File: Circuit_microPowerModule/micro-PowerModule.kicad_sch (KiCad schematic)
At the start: 9 parts, among them J101 Screw_Terminal_01x02, J102 Jack-DC

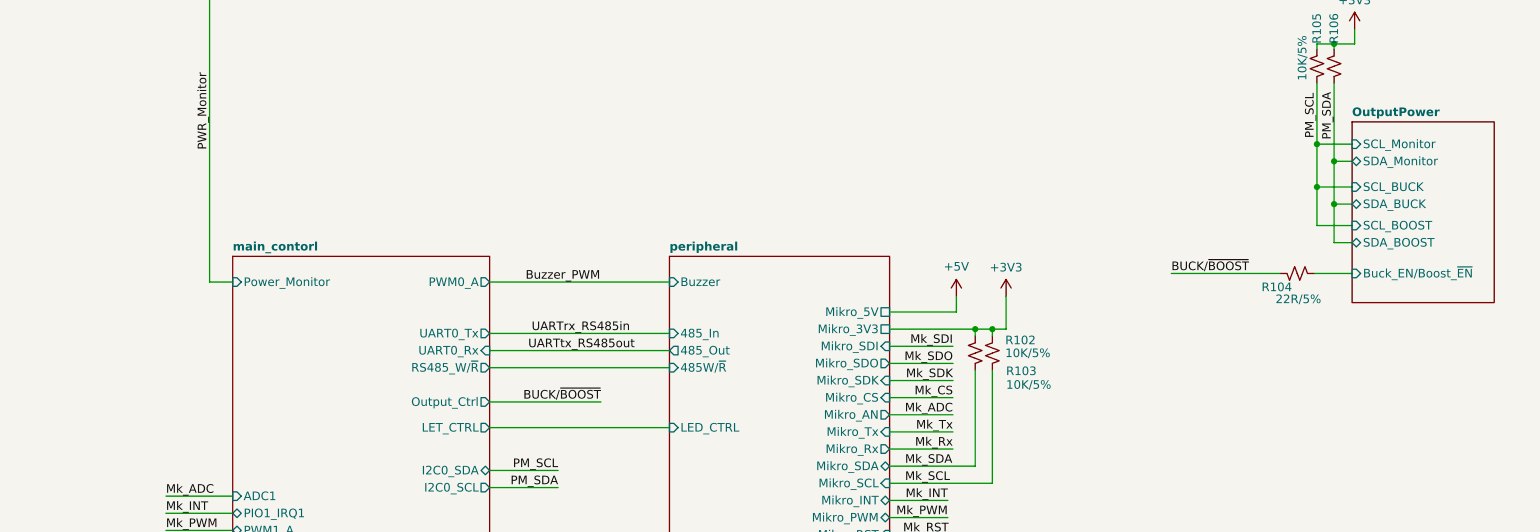
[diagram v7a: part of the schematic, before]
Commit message: added H-Bridge
Control load forward or reverse (current direction)
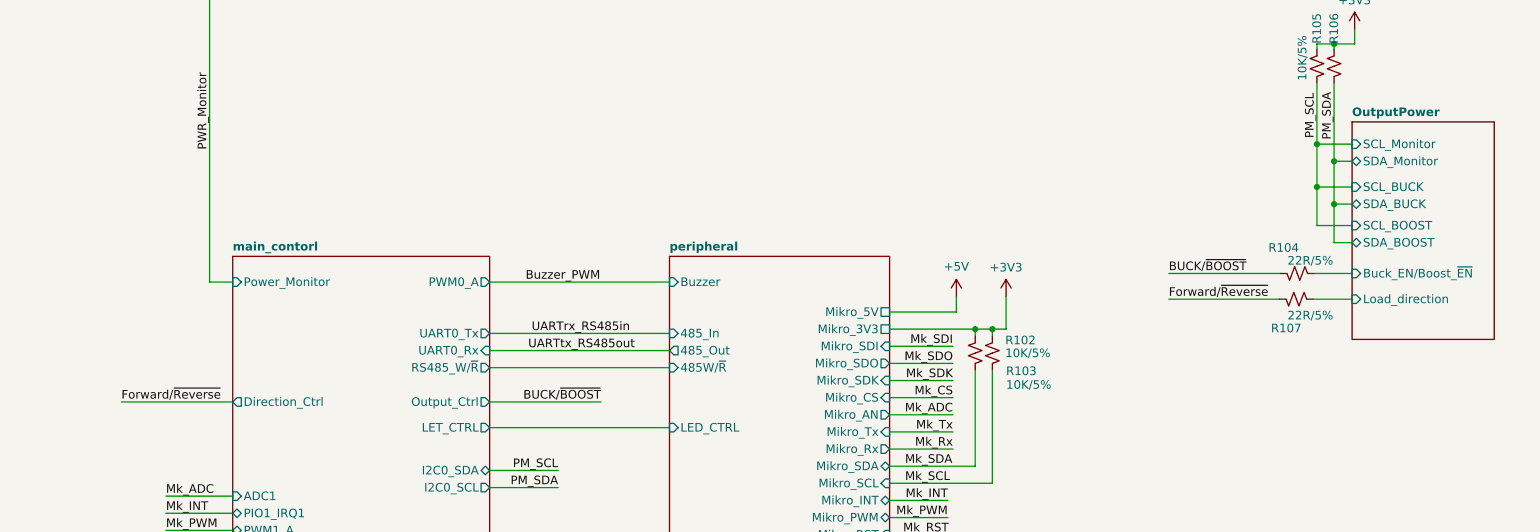
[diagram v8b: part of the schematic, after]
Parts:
- added R107: 22R/5%, Resistor_SMD:R_0603_1608Metric, symbol Device:R_Small_US
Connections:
- new net Forward/~{Reverse}: R107.2
- new net OutputPower/Load_direction: R107.1
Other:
- sheet OutputPower ports: added Load_direction; removed none
- sheet main_contorl ports: added Direction_Ctrl; removed none
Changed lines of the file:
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@@
     (stroke (width 0) (type default))
   )
-  (wire (pts (xy 236.982 82.55) (xy 253.111 82.55))
+  (wire (pts (xy 236.601 82.55) (xy 253.111 82.55))
     (stroke (width 0) (type default))
   )
@@
     (stroke (width 0) (type default))
   )
+  (wire (pts (xy 97.79 101.6) (xy 81.28 101.6))
+    (stroke (width 0) (type default))
+  )
   (wire (pts (xy 135.89 123.19) (xy 162.56 123.19))
     (stroke (width 0) (type default))
@@
     (stroke (width 0) (type default))
   )
+  (wire (pts (xy 236.601 86.36) (xy 252.984 86.36))
+    (stroke (width 0) (type default))
+  )
   (wire (pts (xy 206.248 123.825) (xy 206.248 126.492))
     (stroke (width 0) (type default))
@@
   )
   (wire (pts (xy 261.112 72.263) (xy 263.779 72.263))
+    (stroke (width 0) (type default))
+  )
+  (wire (pts (xy 258.064 86.36) (xy 263.779 86.36))
     (stroke (width 0) (type default))
   )
@@
     (effects (font (size 1.27 1.27)) (justify right bottom))
   )
+  (label "Forward{slash}~{Reverse}" (at 236.601 86.36 0) (fields_autoplaced)
+    (effects (font (size 1.27 1.27)) (justify left bottom))
+  )
   (label "PWR_IN" (at 46.609 46.228 180) (fields_autoplaced)
     (effects (font (size 1.27 1.27)) (justify right bottom))
@@
     (effects (font (size 1.27 1.27)) (justify left bottom))
   )
-  (label "BUCK{slash}~{BOOST}" (at 236.982 82.55 0) (fields_autoplaced)
+  (label "BUCK{slash}~{BOOST}" (at 236.601 82.55 0) (fields_autoplaced)
+    (effects (font (size 1.27 1.27)) (justify left bottom))
+  )
+  (label "Forward{slash}~{Reverse}" (at 81.28 101.6 0) (fields_autoplaced)
     (effects (font (size 1.27 1.27)) (justify left bottom))
   )
@@
   (symbol (lib_id "Device:R_Small_US") (at 255.651 82.55 270) (mirror x) (unit 1)
     (in_bom yes) (on_board yes) (dnp no)
-    (property "Reference" "R104" (at 254.889 84.582 90)
-      (effects (font (size 1.27 1.27)) (justify right))
-    )
-    (property "Value" "22R/5%" (at 259.207 86.36 90)
+    (property "Reference" "R104" (at 255.905 78.74 90)
+      (effects (font (size 1.27 1.27)) (justify right))
+    )
+    (property "Value" "22R/5%" (at 260.985 80.645 90)
       (effects (font (size 1.27 1.27)) (justify right))
     )
@@
     )
   )
+  (symbol (lib_id "Device:R_Small_US") (at 255.524 86.36 270) (mirror x) (unit 1)
+    (in_bom yes) (on_board yes) (dnp no)
+    (property "Reference" "R107" (at 256.286 90.678 90)
+      (effects (font (size 1.27 1.27)) (justify right))
+    )
+    (property "Value" "22R/5%" (at 260.985 88.773 90)
+      (effects (font (size 1.27 1.27)) (justify right))
+    )
+    (property "Footprint" "Resistor_SMD:R_0603_1608Metric" (at 255.524 86.36 0)
+      (effects (font (size 1.27 1.27)) hide)
+    )
+    (property "Datasheet" "~" (at 255.524 86.36 0)
+      (effects (font (size 1.27 1.27)) hide)
+    )
+    (pin "1")
+    (pin "2")
+    (instances
+      (project "micro-PowerModule"
+        (path "/38b19d1a-a8d3-49c0-a6a2-bee4e845832f"
+          (reference "R107") (unit 1)
+        )
+        (path "/38b19d1a-a8d3-49c0-a6a2-bee4e845832f/4d2335ad-4917-40e3-b9fc-5e8d69783b2a"
+          (reference "R35") (unit 1)
+        )
+      )
+    )
+  )
   (symbol (lib_id "power:GNDPWR") (at 46.736 36.957 0) (unit 1)
     (in_bom yes) (on_board yes) (dnp no)
@@
     )
   )
-  (sheet (at 263.779 60.071) (size 21.082 26.797) (fields_autoplaced)
+  (sheet (at 263.779 60.071) (size 21.082 32.258) (fields_autoplaced)
     (stroke (width 0.1524) (type solid))
     (fill (color 0 0 0 0.0000))
@@
       (effects (font (size 1.27 1.27) bold) (justify left bottom))
     )
-    (property "Sheetfile" "OutputPower.kicad_sch" (at 263.779 87.4526 0)
+    (property "Sheetfile" "OutputPower.kicad_sch" (at 263.779 92.9136 0)
       (effects (font (size 1.27 1.27)) (justify left top) hide)
     )
@@
     )
     (pin "Buck_EN{slash}Boost_~{EN}" input (at 263.779 82.55 180)
+      (effects (font (size 1.27 1.27)) (justify left))
+    )
+    (pin "Load_direction" input (at 263.779 86.36 180)
       (effects (font (size 1.27 1.27)) (justify left))
     )
@@
       (effects (font (size 1.27 1.27)) (justify right))
     )
-    (instances
+    (pin "Direction_Ctrl" output (at 97.79 101.6 180)
+      (effects (font (size 1.27 1.27)) (justify left))
+    )
+    (instances
